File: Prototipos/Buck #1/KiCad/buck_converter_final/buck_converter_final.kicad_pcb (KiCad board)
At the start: 2 copper layers, 50 x 100 mm, 43 parts, among them J2 Screw_Terminal_01x02, J3 Screw_Terminal_01x02, K1 SANYOU_SRD_Form_C, Q1 NPN, Q2 IRF9540NPBF, Q3 BC548, U1 INA199xxDCK

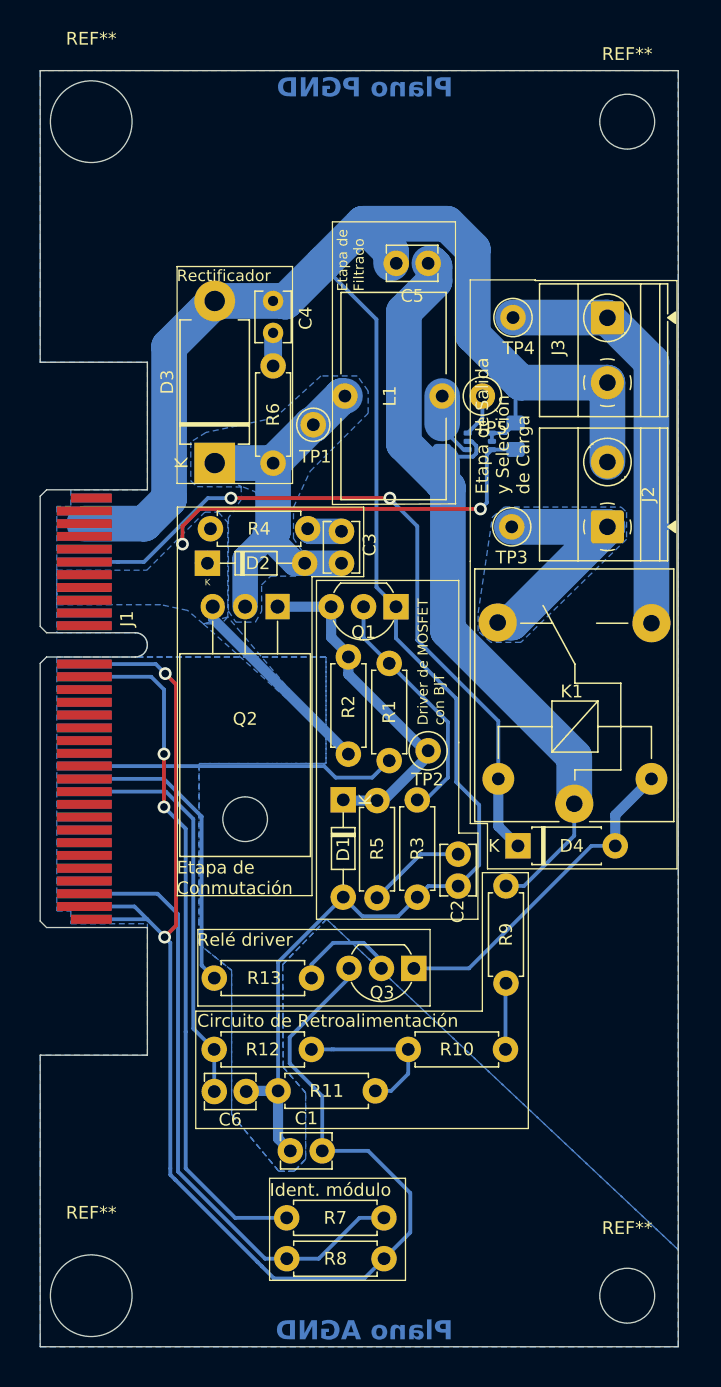
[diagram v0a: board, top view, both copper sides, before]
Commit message: Agregado sensor corriente PCB
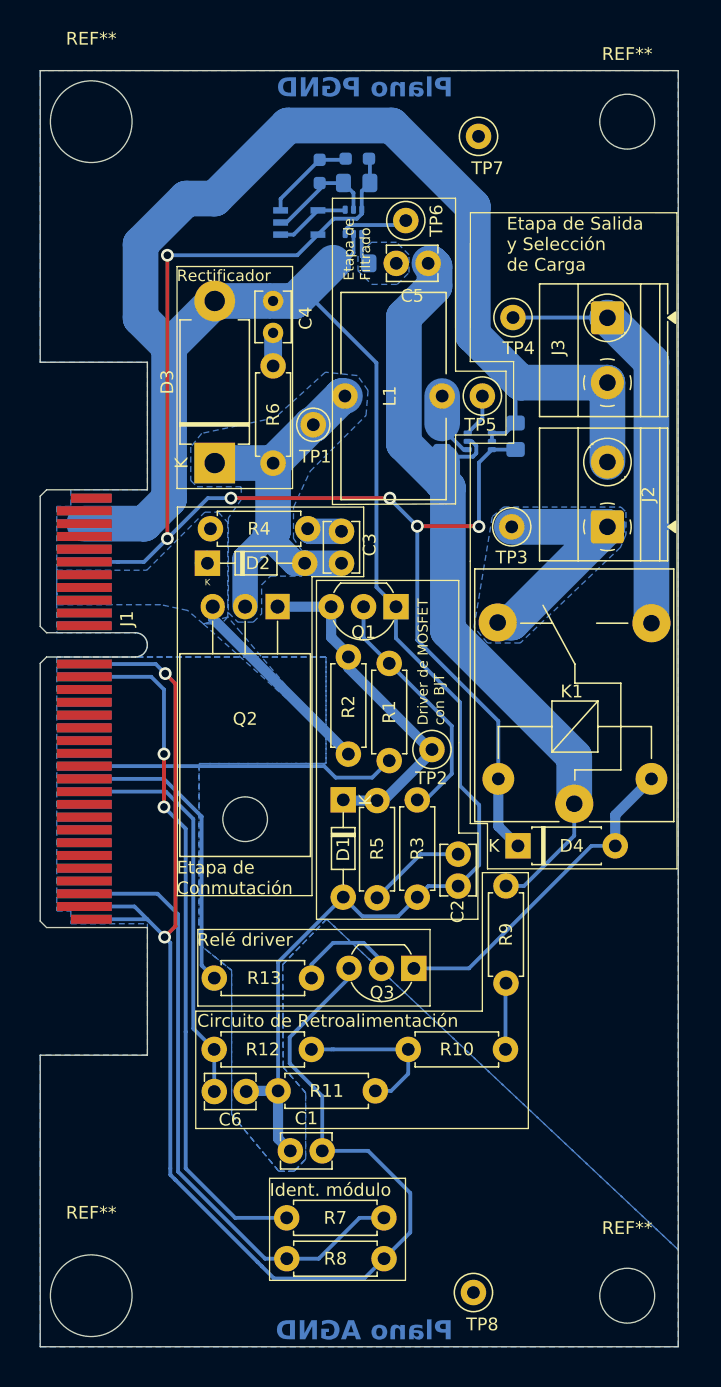
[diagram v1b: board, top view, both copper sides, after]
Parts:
- added C8: 0.1uF, Capacitor_SMD:C_0805_2012Metric_Pad1.18x1.45mm_HandSolder, B.Cu at (129.6, 41.8)
- added R15: 5.1m, Resistor_SMD:R_0805_2012Metric_Pad1.20x1.40mm_HandSolder, B.Cu at (129.6, 48.1)
- added R16: 4.7k, Resistor_SMD:R_0603_1608Metric_Pad0.98x0.95mm_HandSolder, B.Cu at (129.7, 39.9)
- added R17: 4.7k, Resistor_SMD:R_0603_1608Metric_Pad0.98x0.95mm_HandSolder, B.Cu at (126.7, 40.9)
- added TP6: CAPACITOR_CURRENT, TestPoint:TestPoint_Loop_D1.80mm_Drill1.0mm_Beaded, F.Cu at (133.4, 44.8)
- added TP7: PGND, TestPoint:TestPoint_Loop_D1.80mm_Drill1.0mm_Beaded, F.Cu at (139.2, 38.1)
- added TP8: AGND, TestPoint:TestPoint_Loop_D1.80mm_Drill1.0mm_Beaded, F.Cu at (138.8, 128.8)
- added U2: INA199xxDCK, Package_TO_SOT_SMD:SOT-363_SC-70-6, B.Cu at (129.3, 44.9)
- added U4: TL071HIDBVR, TL071H:SOT23_DBV_5_TEX-M, B.Cu at (125.1, 44.9)
- R11: value 4k7 -> 4.7k
- R14: value 0.01 -> 10m
- TP5: value INDUCOR_CURRENT -> INDUCTOR_CURRENT
- moved TP2 0.32 mm to (135.5, 86.2)
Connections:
- net Net-(U1-+) renamed I_CURRENT_+
- net Net-(U1--) renamed I_CURRENT_-
- C5 pad 2: PGND -> C_CURRENT_+
- C7 pad 1: 12V -> 5Vdc
- U1 pad 3: 12V -> 5Vdc
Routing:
- net 5Vdc: track 57.4 -> 114.0 mm, vias 2 -> 6
- net PGND: track 173.4 -> 211.0 mm
- net 12V: track 48.2 -> 16.0 mm, vias 2 -> 0
- net Net-(U4-+): track 0.00 -> 7.30 mm
- net Net-(U2-REF): track 0.00 -> 5.87 mm
- net Net-(TP6-Pad1): track 0.00 -> 5.38 mm
- net C_CURRENT_+: track 0.00 -> 2.53 mm
- added copper zone on B.Cu, net C_CURRENT_+

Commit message: PCB final
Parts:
- moved REF_AGND1 2.90 mm to (139.5, 126.0)
- renumbered TP8 to REF_AGND1, TP7 to REF_PGND1
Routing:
- net PGND: track 211.0 -> 211.5 mm

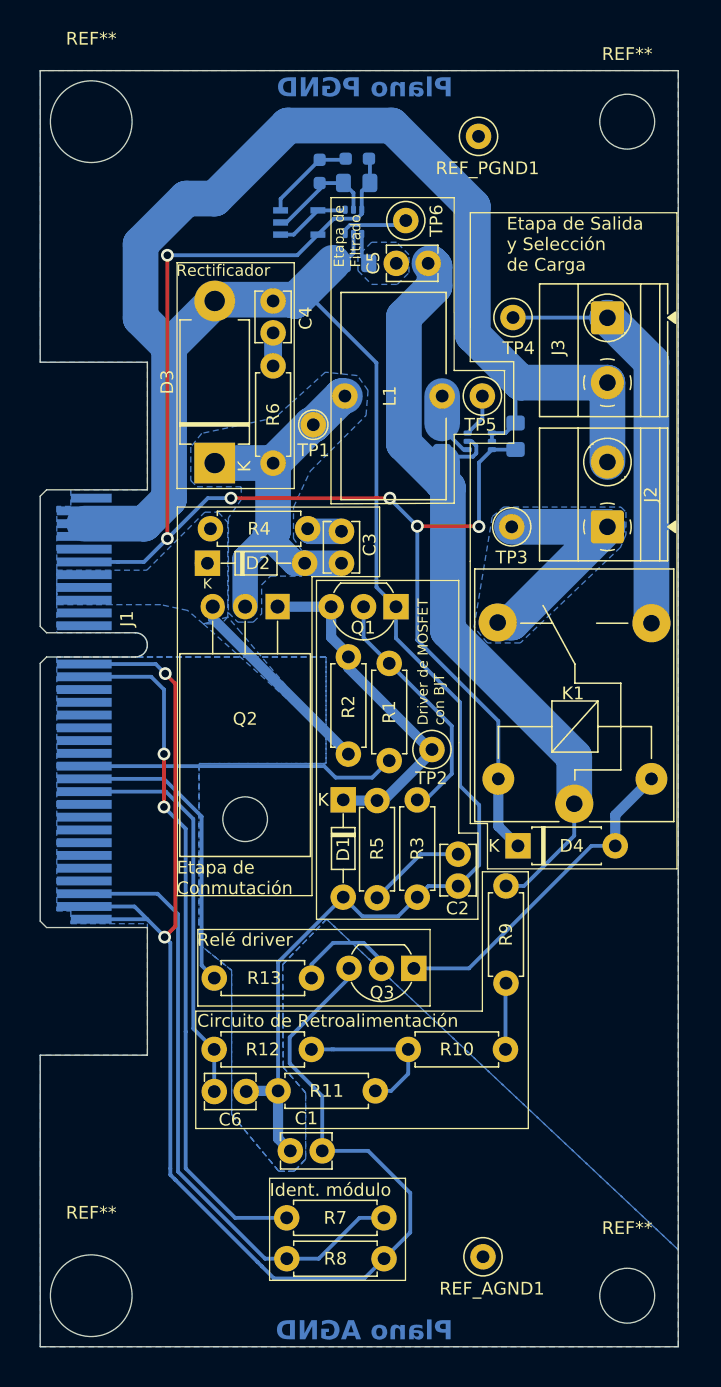
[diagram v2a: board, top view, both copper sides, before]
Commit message: Corregir MHs PCB Buck
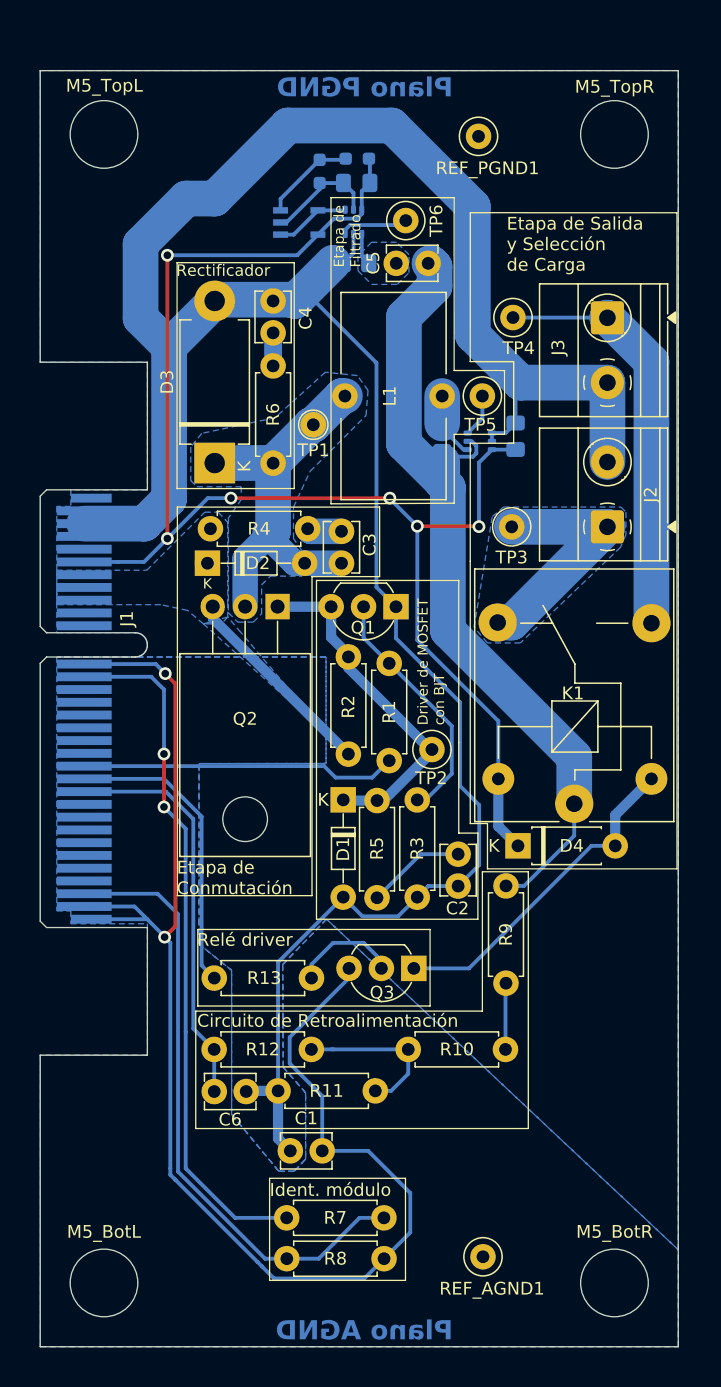
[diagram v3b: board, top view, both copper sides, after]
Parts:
- M5_BotL, M5_TopL: renamed from REF**; value MountingHole_6.4mm_M6_DIN965 -> MountingHole_5.3mm_M5; footprint MountingHole:MountingHole_6.4mm_M6_DIN965 -> MountingHole:MountingHole_5.3mm_M5
- M5_BotR, M5_TopR: renamed from REF**; value MountingHole_4.3mm_M4 -> MountingHole_5.3mm_M5; footprint MountingHole:MountingHole_4.3mm_M4 -> MountingHole:MountingHole_5.3mm_M5
- moved M5_BotL 1.41 mm to (109.8, 128.0)
- moved M5_BotR 1.41 mm to (149.8, 128.0)
- moved M5_TopL 1.41 mm to (109.8, 38.0)
- moved M5_TopR 1.41 mm to (149.8, 38.0)
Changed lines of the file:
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@@
 		)
 	)
-	(footprint "MountingHole:MountingHole_6.4mm_M6_DIN965"
+	(footprint "MountingHole:MountingHole_5.3mm_M5"
 		(locked yes)
 		(layer "F.Cu")
-		(at 108.8 37)
-		(descr "Mounting Hole 6.4mm, no annular, M6, DIN965")
-		(tags "mounting hole 6.4mm no annular m6 din965")
-		(property "Reference" "REF**"
-			(at 0 -6.5 0)
+		(at 109.8 38)
+		(descr "Mounting Hole 5.3mm, M5, no annular, generated by kicad-footprint-generator mountinghole.py")
+		(tags "mountinghole M5")
+		(property "Reference" "M5_TopL"
+			(at 0.033079 -3.818929 0)
 			(layer "F.SilkS")
 			(effects
@@
 			)
 		)
-		(property "Value" "MountingHole_6.4mm_M6_DIN965"
-			(at 0 6.5 0)
+		(property "Value" "MountingHole_5.3mm_M5"
+			(at 0 6.25 0)
 			(layer "F.Fab")
-			(hide yes)
 			(effects
 				(font
@@
 		(property "Datasheet" ""
 			(at 0 0 0)
-			(unlocked yes)
 			(layer "F.Fab")
 			(hide yes)
@@
 		(property "Description" ""
 			(at 0 0 0)
-			(unlocked yes)
 			(layer "F.Fab")
 			(hide yes)
@@
 		(fp_circle
 			(center 0 0)
-			(end 5.5 0)
+			(end 5.3 0)
 			(stroke
 				(width 0.15)
@@
 		(fp_circle
 			(center 0 0)
-			(end 5.75 0)
+			(end 5.55 0)
 			(stroke
 				(width 0.05)
@@
 		(pad "" np_thru_hole circle
 			(at 0 0)
-			(size 6.4 6.4)
-			(drill 6.4)
+			(size 5.3 5.3)
+			(drill 5.3)
 			(layers "*.Cu" "*.Mask")
 		)
@@
 		)
 	)
-	(footprint "MountingHole:MountingHole_4.3mm_M4"
+	(footprint "MountingHole:MountingHole_5.3mm_M5"
 		(locked yes)
 		(layer "F.Cu")
-		(at 150.8 37)
-		(descr "Mounting Hole 4.3mm, no annular, M4")
-		(tags "mounting hole 4.3mm no annular m4")
-		(property "Reference" "REF**"
-			(at 0 -5.3 0)
+		(at 149.8 38)
+		(descr "Mounting Hole 5.3mm, M5, no annular, generated by kicad-footprint-generator mountinghole.py")
+		(tags "mountinghole M5")
+		(property "Reference" "M5_TopR"
+			(at 0.009608 -3.736401 0)
 			(layer "F.SilkS")
 			(effects
@@
 			)
 		)
-		(property "Value" "MountingHole_4.3mm_M4"
-			(at 0 5.3 0)
+		(property "Value" "MountingHole_5.3mm_M5"
+			(at 0 6.25 0)
 			(layer "F.Fab")
 			(effects
@@
 		(property "Datasheet" ""
 			(at 0 0 0)
-			(unlocked yes)
 			(layer "F.Fab")
 			(hide yes)
@@
 		(property "Description" ""
 			(at 0 0 0)
-			(unlocked yes)
 			(layer "F.Fab")
 			(hide yes)
@@
 		(fp_circle
 			(center 0 0)
-			(end 4.3 0)
+			(end 5.3 0)
 			(stroke
 				(width 0.15)
@@
 		(fp_circle
 			(center 0 0)
-			(end 4.55 0)
+			(end 5.55 0)
 			(stroke
 				(width 0.05)
@@
 		(pad "" np_thru_hole circle
 			(at 0 0)
-			(size 4.3 4.3)
-			(drill 4.3)
+			(size 5.3 5.3)
+			(drill 5.3)
 			(layers "*.Cu" "*.Mask")
 		)
@@
 		)
 	)
-	(footprint "MountingHole:MountingHole_6.4mm_M6_DIN965"
+	(footprint "MountingHole:MountingHole_5.3mm_M5"
 		(locked yes)
 		(layer "F.Cu")
-		(at 108.8 129)
-		(descr "Mounting Hole 6.4mm, no annular, M6, DIN965")
-		(tags "mounting hole 6.4mm no annular m6 din965")
-		(property "Reference" "REF**"
-			(at 0 -6.5 0)
+		(at 109.8 128)
+		(descr "Mounting Hole 5.3mm, M5, no annular, generated by kicad-footprint-generator mountinghole.py")
+		(tags "mountinghole M5")
+		(property "Reference" "M5_BotL"
+			(at 0 -4 0)
 			(layer "F.SilkS")
 			(effects
@@
 			)
 		)
-		(property "Value" "MountingHole_6.4mm_M6_DIN965"
-			(at 0 6.5 0)
+		(property "Value" "MountingHole_5.3mm_M5"
+			(at 0 6.25 0)
 			(layer "F.Fab")
-			(hide yes)
 			(effects
 				(font
@@
 		(property "Datasheet" ""
 			(at 0 0 0)
-			(unlocked yes)
 			(layer "F.Fab")
 			(hide yes)
@@
 		(property "Description" ""
 			(at 0 0 0)
-			(unlocked yes)
 			(layer "F.Fab")
 			(hide yes)
@@
 		(fp_circle
 			(center 0 0)
-			(end 5.5 0)
+			(end 5.3 0)
 			(stroke
 				(width 0.15)
@@
 		(fp_circle
 			(center 0 0)
-			(end 5.75 0)
+			(end 5.55 0)
 			(stroke
 				(width 0.05)
@@
 		(pad "" np_thru_hole circle
 			(at 0 0)
-			(size 6.4 6.4)
-			(drill 6.4)
+			(size 5.3 5.3)
+			(drill 5.3)
 			(layers "*.Cu" "*.Mask")
 		)
@@
 		)
 	)
-	(footprint "MountingHole:MountingHole_4.3mm_M4"
+	(footprint "MountingHole:MountingHole_5.3mm_M5"
 		(locked yes)
 		(layer "F.Cu")
-		(at 150.8 129)
-		(descr "Mounting Hole 4.3mm, no annular, M4")
-		(tags "mounting hole 4.3mm no annular m4")
-		(property "Reference" "REF**"
-			(at 0 -5.3 0)
+		(at 149.8 128)
+		(descr "Mounting Hole 5.3mm, M5, no annular, generated by kicad-footprint-generator mountinghole.py")
+		(tags "mountinghole M5")
+		(property "Reference" "M5_BotR"
+			(at 0 -4.003344 0)
 			(layer "F.SilkS")
 			(effects
@@
 			)
 		)
-		(property "Value" "MountingHole_4.3mm_M4"
-			(at 0 5.3 0)
+		(property "Value" "MountingHole_5.3mm_M5"
+			(at 0 6.25 0)
 			(layer "F.Fab")
 			(effects
@@
 		(property "Datasheet" ""
 			(at 0 0 0)
-			(unlocked yes)
 			(layer "F.Fab")
 			(hide yes)
@@
 		(property "Description" ""
 			(at 0 0 0)
-			(unlocked yes)
 			(layer "F.Fab")
 			(hide yes)
@@
 		(fp_circle
 			(center 0 0)
-			(end 4.3 0)
+			(end 5.3 0)
 			(stroke
 				(width 0.15)
@@
 		(fp_circle
 			(center 0 0)
-			(end 4.55 0)
+			(end 5.55 0)
 			(stroke
 				(width 0.05)
@@
 		)
 		(fp_text user "${REFERENCE}"
-			(at 0 0 0)
+			(at 0.006333 -4 0)
 			(layer "F.Fab")
 			(effects
@@
 		(pad "" np_thru_hole circle
 			(at 0 0)
-			(size 4.3 4.3)
-			(drill 4.3)
+			(size 5.3 5.3)
+			(drill 5.3)
 			(layers "*.Cu" "*.Mask")
 		)

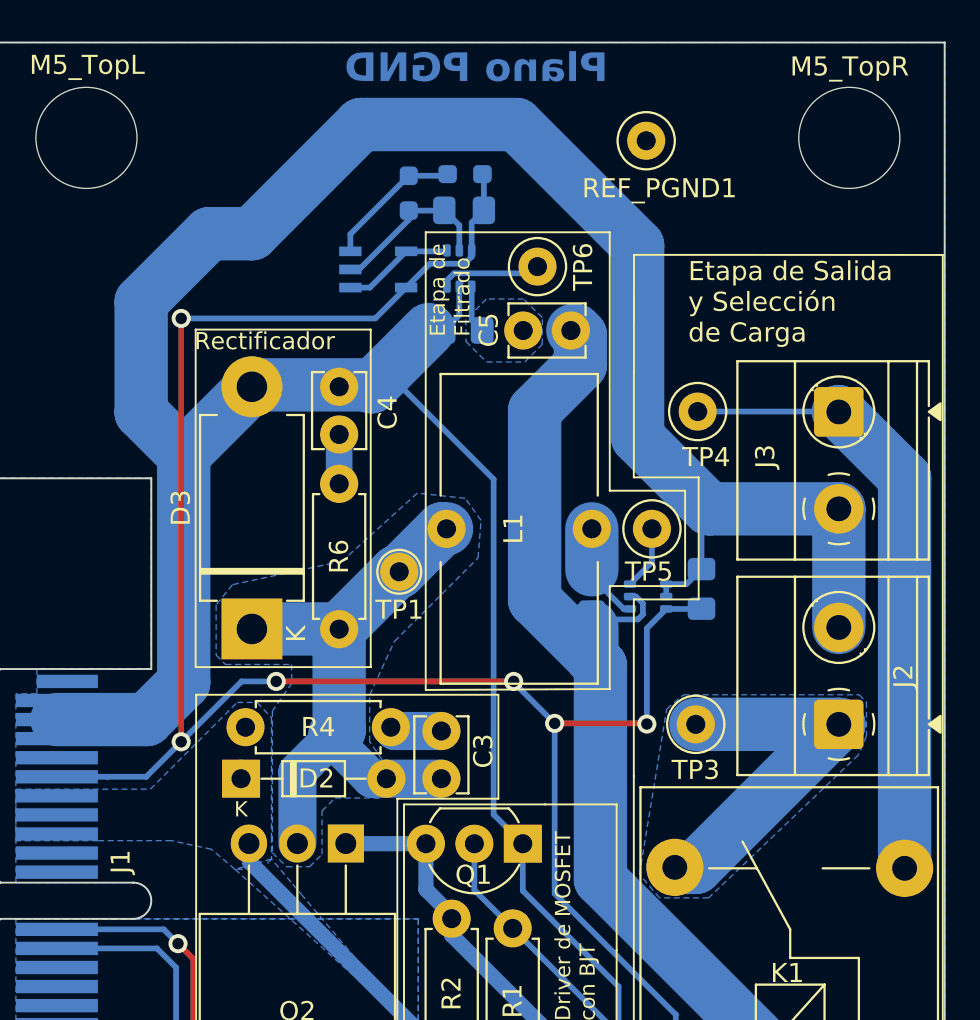
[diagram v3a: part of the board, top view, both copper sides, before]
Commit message: Actualizar huella resistencia shunt
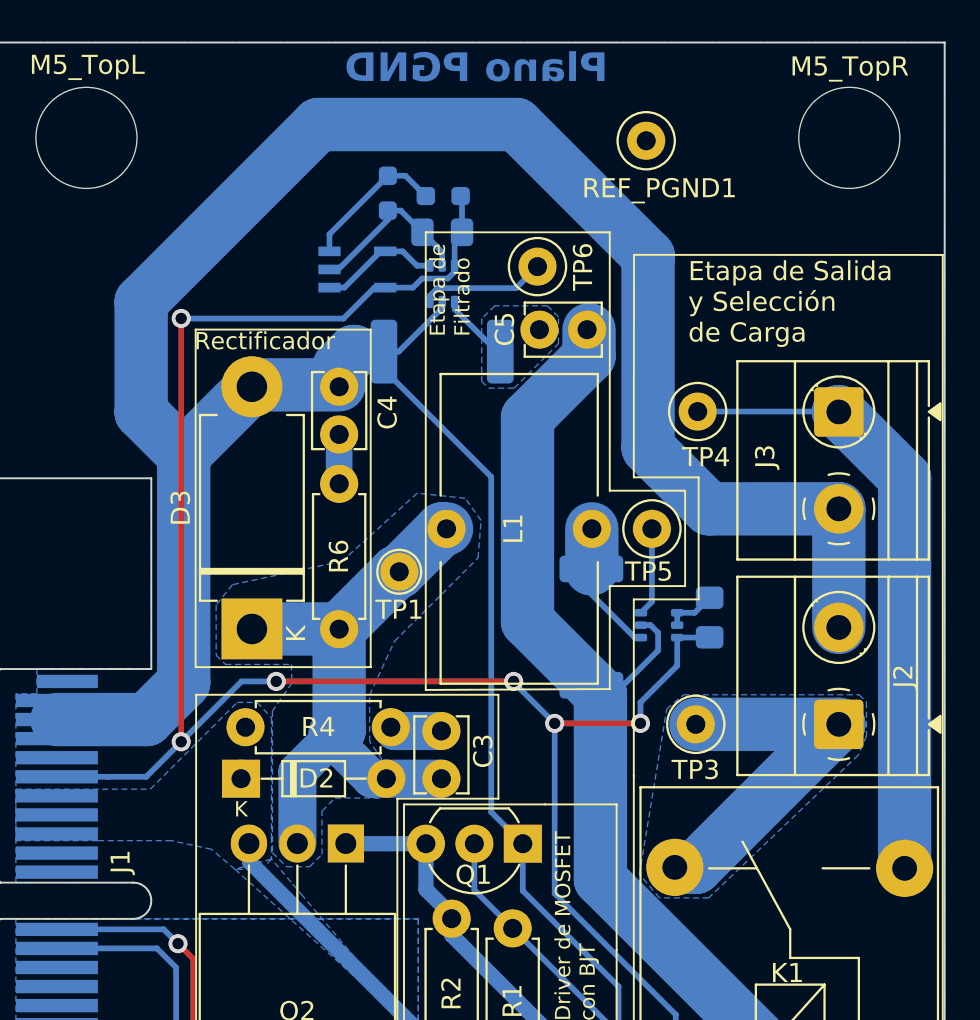
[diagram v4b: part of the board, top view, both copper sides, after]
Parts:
- R14: footprint Resistor_SMD:R_0805_2012Metric_Pad1.20x1.40mm_HandSolder -> Resistor_SMD:R_2512_6332Metric_Pad1.40x3.35mm_HandSolder
- R15: value 5.1m -> 5m; footprint Resistor_SMD:R_0805_2012Metric_Pad1.20x1.40mm_HandSolder -> Resistor_SMD:R_2512_6332Metric_Pad1.40x3.35mm_HandSolder
- moved R14 1.80 mm to (136.3, 63.6)
- moved R16 1.62 mm to (128.5, 41.0)
- moved C8 1.62 mm to (128.5, 43.0)
- moved U1 1.61 mm to (139.8, 63.5)
- moved R15 1.56 mm to (128.4, 49.2)
- moved C7 1.56 mm to (142.5, 63.1)
- moved U2 1.20 mm to (128.5, 45.6)
- moved R17 1.10 mm to (125.6, 40.9)
- moved U4 1.10 mm to (124.0, 44.9)
- moved C5 0.85 mm to (136.1, 48.1)
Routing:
- net PGND: track 211.5 -> 205.7 mm
- net 5Vdc: track 114.0 -> 110.6 mm
- net I_CURRENT_+: track 5.02 -> 6.98 mm
- net Net-(TP5-Pad1): track 3.38 -> 4.64 mm
- net Net-(TP6-Pad1): track 5.38 -> 6.60 mm
- net C_CURRENT_+: track 2.53 -> 3.70 mm
- net I_CURRENT_-: track 64.5 -> 65.1 mm
